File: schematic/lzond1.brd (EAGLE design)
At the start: 100 x 80 mm, 16 parts, among them IC1 786TV

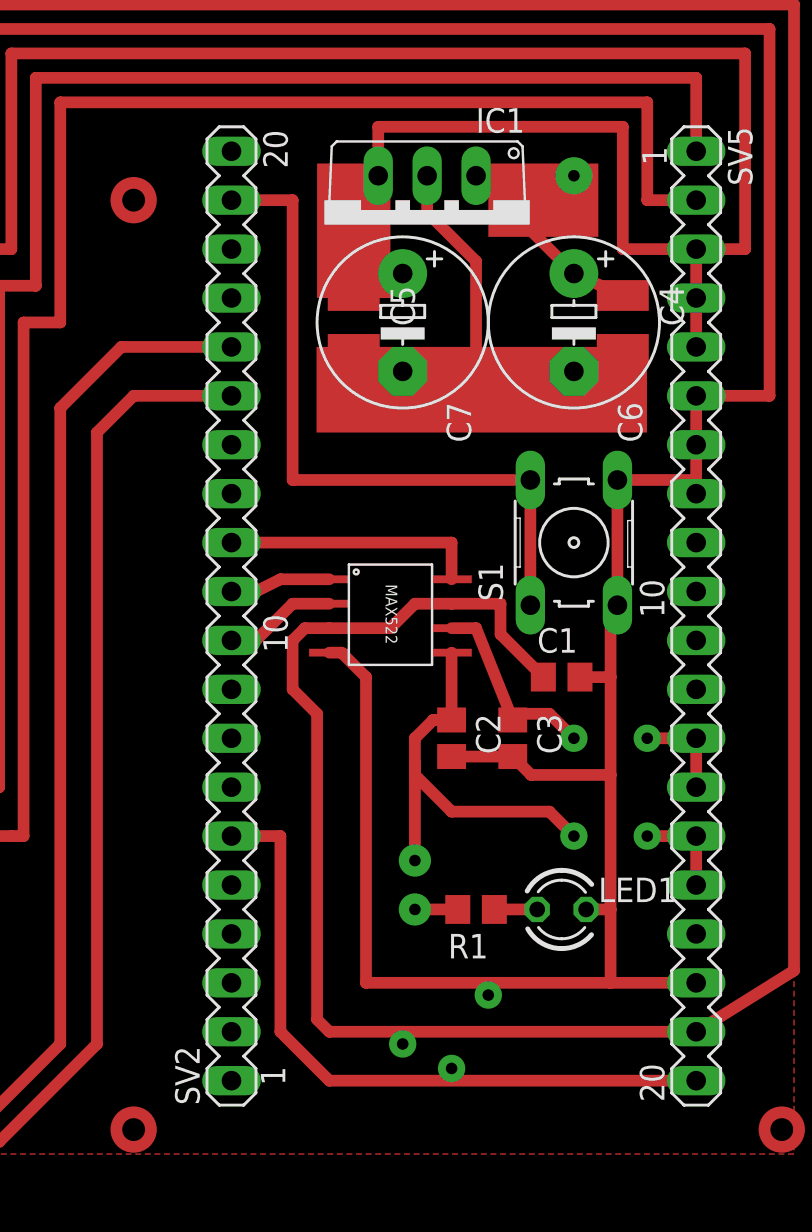
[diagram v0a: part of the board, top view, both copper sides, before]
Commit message: Fixed bug in mix definition
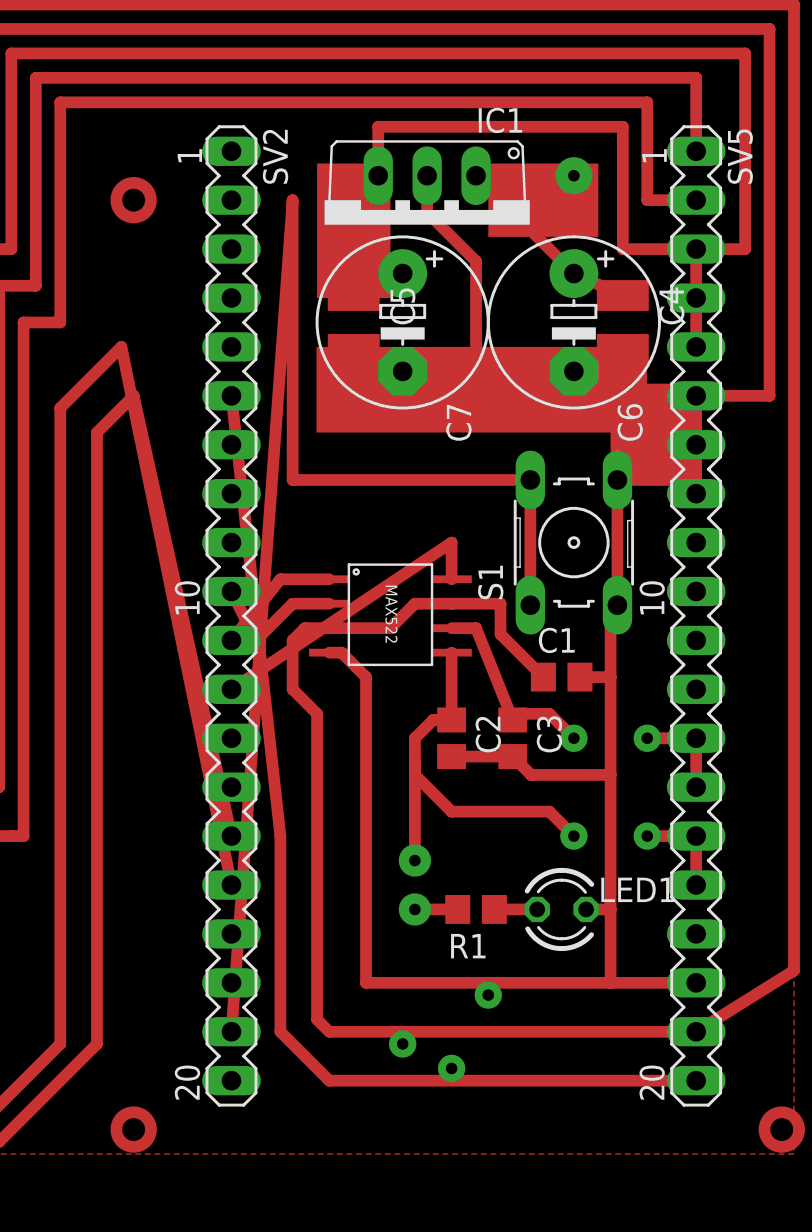
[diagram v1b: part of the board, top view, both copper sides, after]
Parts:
- turned SV2 to 270 degrees
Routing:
- net N$16: track 36.6 -> 76.7 mm
- net N$9: track 75.5 -> 98.3 mm
- net N$18: track 35.3 -> 55.8 mm
- net N$10: track 70.0 -> 88.4 mm
- net N$13: track 13.3 -> 15.6 mm
- net N$15: track 5.87 -> 7.44 mm
- net N$14: track 5.23 -> 6.61 mm
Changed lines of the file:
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@@
 <layers>
 <layer number="1" name="Top" color="4" fill="1" visible="yes" active="yes"/>
-<layer number="16" name="Bottom" color="1" fill="1" visible="no" active="yes"/>
+<layer number="16" name="Bottom" color="1" fill="1" visible="yes" active="yes"/>
 <layer number="17" name="Pads" color="2" fill="1" visible="yes" active="yes"/>
 <layer number="18" name="Vias" color="2" fill="1" visible="yes" active="yes"/>
-<layer number="19" name="Unrouted" color="6" fill="1" visible="no" active="yes"/>
-<layer number="20" name="Dimension" color="15" fill="1" visible="no" active="yes"/>
-<layer number="21" name="tPlace" color="7" fill="1" visible="no" active="yes"/>
-<layer number="22" name="bPlace" color="7" fill="1" visible="no" active="yes"/>
-<layer number="23" name="tOrigins" color="15" fill="1" visible="no" active="yes"/>
-<layer number="24" name="bOrigins" color="15" fill="1" visible="no" active="yes"/>
-<layer number="25" name="tNames" color="7" fill="1" visible="no" active="yes"/>
-<layer number="26" name="bNames" color="7" fill="1" visible="no" active="yes"/>
-<layer number="27" name="tValues" color="7" fill="1" visible="no" active="yes"/>
-<layer number="28" name="bValues" color="7" fill="1" visible="no" active="yes"/>
+<layer number="19" name="Unrouted" color="6" fill="1" visible="yes" active="yes"/>
+<layer number="20" name="Dimension" color="15" fill="1" visible="yes" active="yes"/>
+<layer number="21" name="tPlace" color="7" fill="1" visible="yes" active="yes"/>
+<layer number="22" name="bPlace" color="7" fill="1" visible="yes" active="yes"/>
+<layer number="23" name="tOrigins" color="15" fill="1" visible="yes" active="yes"/>
+<layer number="24" name="bOrigins" color="15" fill="1" visible="yes" active="yes"/>
+<layer number="25" name="tNames" color="7" fill="1" visible="yes" active="yes"/>
+<layer number="26" name="bNames" color="7" fill="1" visible="yes" active="yes"/>
+<layer number="27" name="tValues" color="7" fill="1" visible="yes" active="yes"/>
+<layer number="28" name="bValues" color="7" fill="1" visible="yes" active="yes"/>
 <layer number="29" name="tStop" color="7" fill="3" visible="no" active="yes"/>
 <layer number="30" name="bStop" color="7" fill="6" visible="no" active="yes"/>
@@
 <circle x="45.72" y="15.24" radius="0.898025" width="0.6096" layer="1"/>
 <circle x="31.75" y="69.85" radius="0.898025" width="0.6096" layer="1"/>
+<rectangle x1="70.485" y1="48.895" x2="74.93" y2="53.975" layer="1"/>
 </plain>
 <attributes>
@@
 <attribute name="OC_FARNELL" value="unknown" x="35.56" y="41.91" size="1.778" layer="27" rot="R90" display="off"/>
 </element>
-<element name="SV2" library="con-lstb" package="MA20-1" value="" x="50.8" y="41.91" rot="R90">
-<attribute name="OC_NEWARK" value="unknown" x="50.8" y="41.91" size="1.778" layer="27" rot="R90" display="off"/>
-<attribute name="MPN" value="" x="50.8" y="41.91" size="1.778" layer="27" rot="R90" display="off"/>
-<attribute name="MF" value="" x="50.8" y="41.91" size="1.778" layer="27" rot="R90" display="off"/>
-<attribute name="OC_FARNELL" value="unknown" x="50.8" y="41.91" size="1.778" layer="27" rot="R90" display="off"/>
+<element name="SV2" library="con-lstb" package="MA20-1" value="" x="50.8" y="41.91" rot="R270">
+<attribute name="OC_NEWARK" value="unknown" x="50.8" y="41.91" size="1.778" layer="27" rot="R270" display="off"/>
+<attribute name="MPN" value="" x="50.8" y="41.91" size="1.778" layer="27" rot="R270" display="off"/>
+<attribute name="MF" value="" x="50.8" y="41.91" size="1.778" layer="27" rot="R270" display="off"/>
+<attribute name="OC_FARNELL" value="unknown" x="50.8" y="41.91" size="1.778" layer="27" rot="R270" display="off"/>
 </element>
 <element name="SV3" library="con-lstb" package="MA20-1" value="" x="22.86" y="41.91" rot="R270">
@@
 <wire x1="41.91" y1="19.685" x2="41.91" y2="52.705" width="0.6096" layer="1"/>
 <wire x1="41.91" y1="52.705" x2="45.085" y2="55.88" width="0.6096" layer="1"/>
-<wire x1="45.085" y1="55.88" x2="50.8" y2="55.88" width="0.6096" layer="1"/>
+<wire x1="45.085" y1="55.88" x2="50.8" y2="27.94" width="0.6096" layer="1"/>
 </signal>
 <signal name="N$10">
@@
 <wire x1="43.815" y1="19.685" x2="43.815" y2="51.435" width="0.6096" layer="1"/>
 <wire x1="43.815" y1="51.435" x2="45.72" y2="53.34" width="0.6096" layer="1"/>
-<wire x1="45.72" y1="53.34" x2="50.8" y2="53.34" width="0.6096" layer="1"/>
+<wire x1="45.72" y1="53.34" x2="50.8" y2="30.48" width="0.6096" layer="1"/>
 </signal>
 <signal name="N$13">
@@
 <contactref element="U$2" pad="DIN"/>
 <wire x1="62.23" y1="43.815" x2="62.23" y2="45.72" width="0.6096" layer="1"/>
-<wire x1="62.23" y1="45.72" x2="50.8" y2="45.72" width="0.6096" layer="1"/>
+<wire x1="62.23" y1="45.72" x2="50.8" y2="38.1" width="0.6096" layer="1"/>
 </signal>
 <signal name="N$14">
@@
 <contactref element="U$2" pad="CS"/>
 <wire x1="55.88" y1="43.815" x2="53.34" y2="43.815" width="0.6096" layer="1"/>
-<wire x1="53.34" y1="43.815" x2="52.07" y2="43.18" width="0.6096" layer="1"/>
-<wire x1="52.07" y1="43.18" x2="50.8" y2="43.18" width="0.6096" layer="1"/>
+<wire x1="53.34" y1="43.815" x2="50.8" y2="40.64" width="0.6096" layer="1"/>
 </signal>
 <signal name="N$15">
@@
 <wire x1="55.88" y1="42.545" x2="53.975" y2="42.545" width="0.6096" layer="1"/>
 <wire x1="53.975" y1="42.545" x2="52.07" y2="40.64" width="0.6096" layer="1"/>
-<wire x1="52.07" y1="40.64" x2="50.8" y2="40.64" width="0.6096" layer="1"/>
+<wire x1="52.07" y1="40.64" x2="50.8" y2="43.18" width="0.6096" layer="1"/>
 </signal>
 <signal name="N$16">
@@
 <contactref element="SV2" pad="19"/>
 <contactref element="S1" pad="1"/>
-<wire x1="50.8" y1="63.5" x2="53.975" y2="63.5" width="0.6096" layer="1"/>
+<wire x1="50.8" y1="20.32" x2="53.975" y2="63.5" width="0.6096" layer="1"/>
 <wire x1="53.975" y1="63.5" x2="53.975" y2="48.9712" width="0.6096" layer="1"/>
 <wire x1="66.3194" y1="42.4688" x2="66.3194" y2="48.9712" width="0.6096" layer="1"/>
@@
 <contactref element="SV2" pad="6"/>
 <contactref element="SV5" pad="20"/>
-<wire x1="50.8" y1="30.48" x2="53.34" y2="30.48" width="0.6096" layer="1"/>
+<wire x1="50.8" y1="53.34" x2="53.34" y2="30.48" width="0.6096" layer="1"/>
 <wire x1="53.34" y1="30.48" x2="53.34" y2="20.32" width="0.6096" layer="1"/>
 <wire x1="53.34" y1="20.32" x2="55.88" y2="17.78" width="0.6096" layer="1"/>
